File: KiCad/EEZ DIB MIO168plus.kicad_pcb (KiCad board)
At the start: 4 copper layers, 191 x 95 mm, 277 parts, among them IC1 USB3300-EZK, IC10 MC78L15ACDR2G, IC11 MC79L15ACDR2G, IC12 74HC126PW,118, IC13 OPA2196IDR, IC14 DAC7760IPWPR, IC15 DAC7760IPWPR, IC16 SN74LVC138ADBR, IC17 DAC7563TDGSR, IC18 OPA376AIDBVR, IC19 PCAL9714HNMP, IC2 M24C32-DFDW6TP, IC20 OPA2196IDR, IC21 TLE75008ESDXUMA1, IC22 TL431B, IC3 ISO6762FDWR, IC4 ISO6762FDWR, IC5 ISO6762FDWR, IC6 STM32F446ZET6, IC7 IS42S16400N-6TL, IC8 SN6505BDBVT, IC9 TPS7A2033PDBVR, Q1 MMBT5401, Q10 NTJD5121NT1G, Q11 NTJD5121NT1G, Q2 MMBT5551, Q3 MMBT5551, Q4 DMP3099L, Q5 2N7002, Q6 DMP3099L, Q7 NTJD5121NT1G, Q8 NTJD5121NT1G, Q9 NTJD5121NT1G, X2 CBED202-1379B001C1AD, X4 1844824, Y1 ABM8-16.000MHZ-10-D7G-T

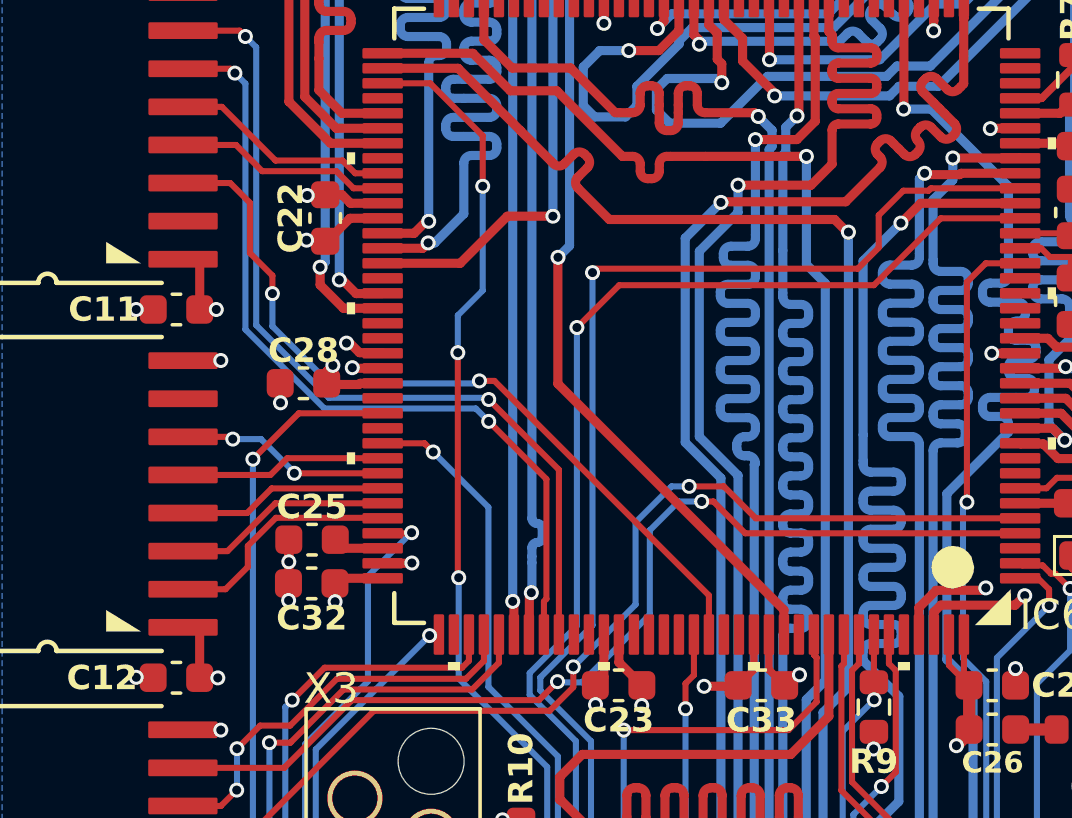
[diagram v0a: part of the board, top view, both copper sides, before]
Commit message: DIB_SYNC added to isolator (currently not used)
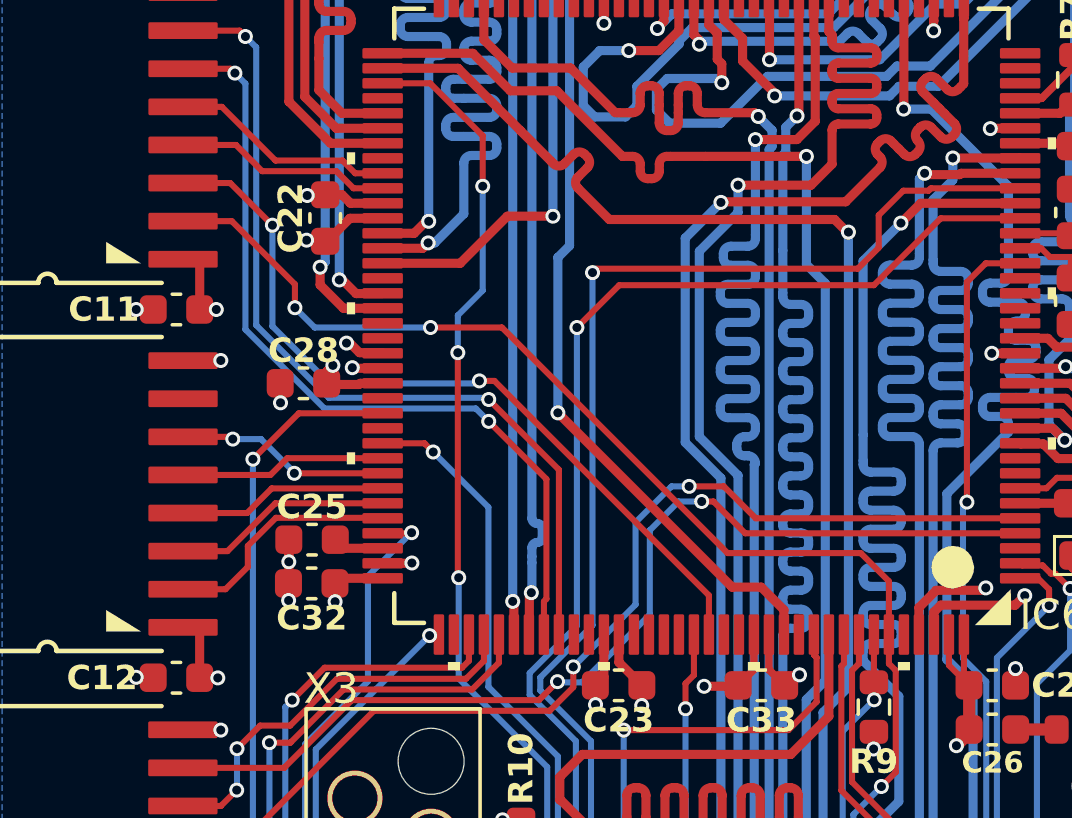
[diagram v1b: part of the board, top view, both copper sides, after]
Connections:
- IC4 pad 2: unconnected-(IC4-INA-Pad2) -> DIB_SYNC
- IC6 pad 139: DIB_OE_SYNC -> DIB_SYNC
- X1 pad B13: DIB_OE_SYNC -> DIB_SYNC
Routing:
- net DIB_SYNC: track 0.00 -> 145.6 mm, vias 0 -> 4
- net DIB_OE_SYNC: track 114.9 -> 0.00 mm, vias 2 -> 0
- net /MCU, SDRAM/FMC_SDNCAS: track 42.9 -> 43.4 mm

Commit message: Gerbers updated
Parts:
- moved C16 1.47 mm to (250.5, 105.4)
- moved C17 1.46 mm to (249.1, 105.4)
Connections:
- net /MCU, SDRAM/RCC_OSC_OUT renamed Net-(IC6B-PH1-OSC_OUT)
- C34 pad 2: /MCU, SDRAM/RCC_OSC_IN -> CLK_IN
- IC6 pad 23: /MCU, SDRAM/RCC_OSC_IN -> CLK_IN
- X1 pad B17: unconnected-(X1-A2-PadB17) -> CLK_IN
- Y1 pad 1: /MCU, SDRAM/RCC_OSC_IN -> CLK_IN
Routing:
- net CLK_IN: track 0.00 -> 140.5 mm, vias 0 -> 2
- net GND: track 114.8 -> 103.8 mm
- net /MCU, SDRAM/RCC_OSC_IN: track 6.21 -> 0.00 mm
